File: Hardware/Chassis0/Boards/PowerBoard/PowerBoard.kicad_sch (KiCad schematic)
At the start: 37 parts, among them IC1 ACS772ECB-400B-PFF-T, IC2 ACS772ECB-400B-PFF-T, IC3 ACS772ECB-400B-PFF-T, IC4 ACS772ECB-400B-PFF-T, J1 Conn_02x08_Counter_Clockwise, J2 7466205R, J3 7466205R, J4 7466205R, J5 Conn_02x08_Counter_Clockwise, J6 7466205R, J7 Conn_02x08_Counter_Clockwise, J8 7466205R, J9 Conn_02x08_Counter_Clockwise, U1 LMT87DCK

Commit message: Add power stage wip design for size 0
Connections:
- net NTC_C: now also J9.16 (Pin_16)
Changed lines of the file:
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@@
 	)
 	(label "NTC_C"
-		(at 27.94 39.37 180)
+		(at 29.21 39.37 180)
 		(effects
 			(font

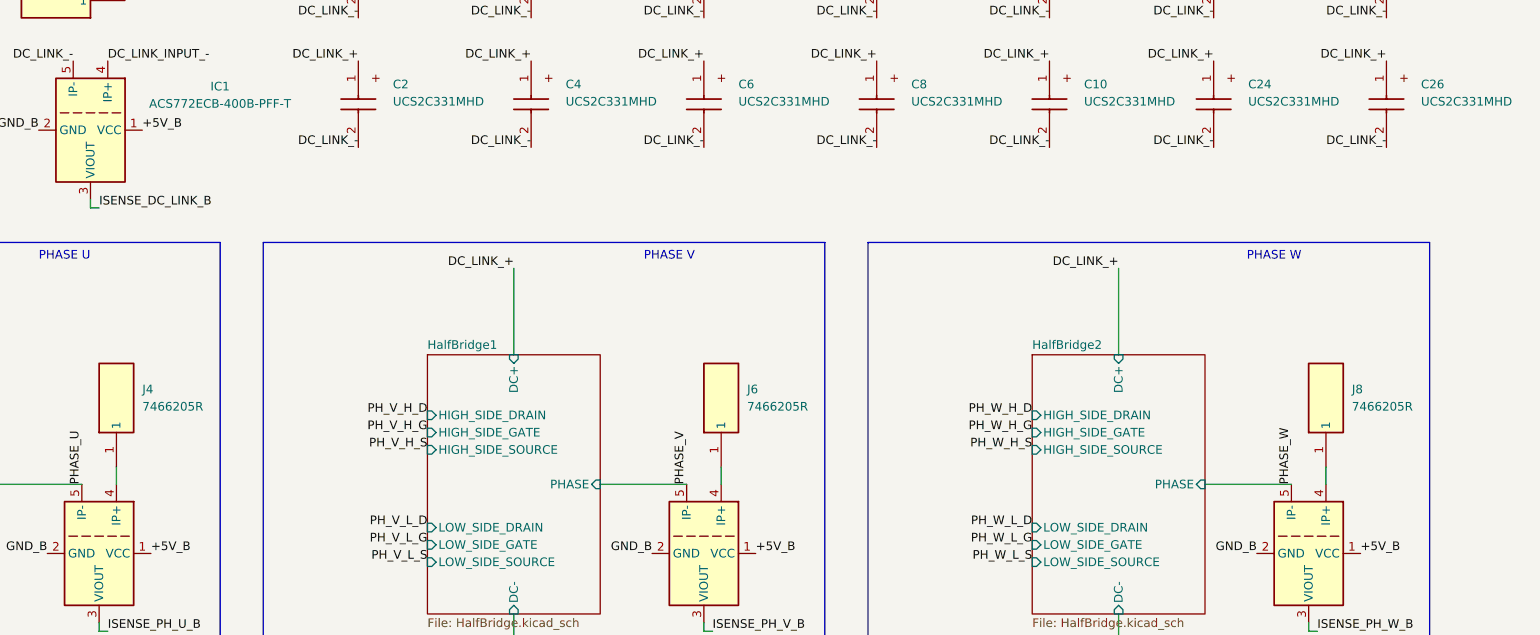
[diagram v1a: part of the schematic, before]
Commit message: Add control board outline for size 0
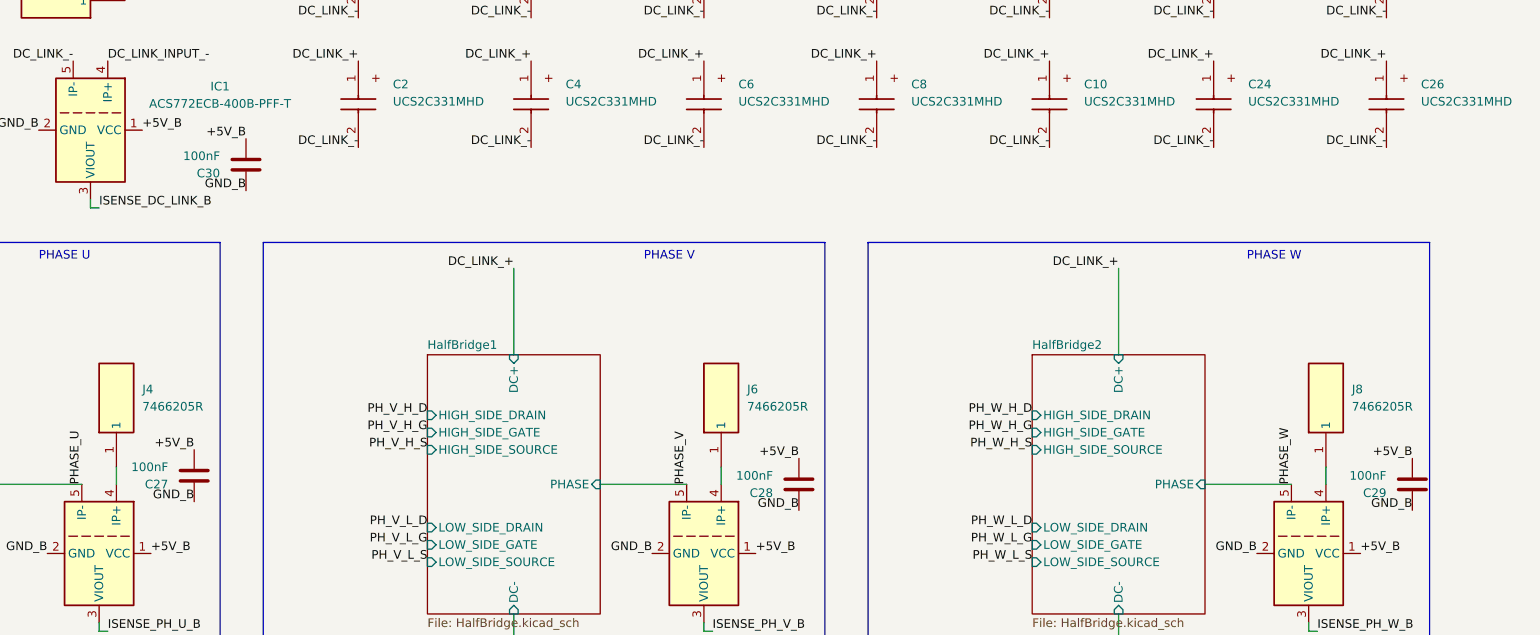
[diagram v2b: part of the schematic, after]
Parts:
- added C27, C28, C29, C30: 100nF, Capacitor_SMD:C_1210_3225Metric_Pad1.33x2.70mm_HandSolder, symbol Device:C
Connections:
- net +5V_B: now also C27.2, C28.2, C29.2, C30.2
- net GND_B: now also C27.1, C28.1, C29.1, C30.1
